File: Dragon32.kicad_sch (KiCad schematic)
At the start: 5 parts, among them IC25 LM393P, IC31 74LS02N

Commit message: rework board
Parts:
- IC31: value 74LS02N -> 74ACT02; footprint Package_DIP:DIP-14_W7.62mm -> Package_SO:SOIC-14_3.9x8.7mm_P1.27mm; DigiKey 296-1627-5-ND -> MC74ACT02DR2GOSCT-ND
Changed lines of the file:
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@@
       (effects (font (size 1.27 1.27)) (justify left))
     )
-    (property "Value" "74LS02N" (at 71.755 51.1809 0)
+    (property "Value" "74ACT02" (at 71.755 51.1809 0)
       (effects (font (size 1.27 1.27)) (justify left))
     )
-    (property "Footprint" "Package_DIP:DIP-14_W7.62mm" (at 65.913 49.911 0)
+    (property "Footprint" "Package_SO:SOIC-14_3.9x8.7mm_P1.27mm" (at 65.913 49.911 0)
       (effects (font (size 1.27 1.27)) hide)
     )
@@
       (effects (font (size 1.27 1.27)) hide)
     )
-    (property "DigiKey" "296-1627-5-ND" (at 65.913 49.911 0)
+    (property "DigiKey" "MC74ACT02DR2GOSCT-ND" (at 65.913 49.911 0)
       (effects (font (size 1.27 1.27)) hide)
     )

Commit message: serial wiring
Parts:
- IC1: renamed from IC25; value LM393P -> LM393DR; footprint Package_DIP:DIP-8_W7.62mm -> Package_SO:SOP-8_3.9x4.9mm_P1.27mm; DigiKey 296-1398-5-ND -> 296-1015-1-ND
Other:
- added sheet Serial (serial.kicad_sch)
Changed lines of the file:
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@@
   (symbol (lib_id "Comparator:LM393") (at 98.425 51.054 0) (unit 3)
     (in_bom yes) (on_board yes) (dnp no) (fields_autoplaced)
-    (property "Reference" "IC25" (at 96.52 49.7839 0)
-      (effects (font (size 1.27 1.27)) (justify left))
-    )
-    (property "Value" "LM393P" (at 96.52 52.3239 0)
-      (effects (font (size 1.27 1.27)) (justify left))
-    )
-    (property "Footprint" "Package_DIP:DIP-8_W7.62mm" (at 98.425 51.054 0)
+    (property "Reference" "IC1" (at 96.52 49.7839 0)
+      (effects (font (size 1.27 1.27)) (justify left))
+    )
+    (property "Value" "LM393DR" (at 96.52 52.3239 0)
+      (effects (font (size 1.27 1.27)) (justify left))
+    )
+    (property "Footprint" "Package_SO:SOP-8_3.9x4.9mm_P1.27mm" (at 98.425 51.054 0)
       (effects (font (size 1.27 1.27)) hide)
     )
@@
       (effects (font (size 1.27 1.27)) hide)
     )
-    (property "DigiKey" "296-1398-5-ND" (at 98.425 51.054 0)
+    (property "DigiKey" "296-1015-1-ND" (at 98.425 51.054 0)
       (effects (font (size 1.27 1.27)) hide)
     )
@@
       (project "Dragon32"
         (path "/0c3dceba-7c95-4b3d-b590-0eb581444beb"
-          (reference "IC25") (unit 3)
+          (reference "IC1") (unit 3)
         )
       )
@@
       (effects (font (size 1.27 1.27)) (justify left top))
     )
+    (instances
+      (project "Dragon32"
+        (path "/0c3dceba-7c95-4b3d-b590-0eb581444beb" (page "8"))
+      )
+    )
+  )
+  (sheet (at 361.188 184.15) (size 26.924 19.812) (fields_autoplaced)
+    (stroke (width 0.1524) (type solid))
+    (fill (color 0 0 0 0.0000))
+    (property "Sheetname" "Serial" (at 361.188 183.4384 0)
+      (effects (font (size 1.27 1.27)) (justify left bottom))
+    )
+    (property "Sheetfile" "serial.kicad_sch" (at 361.188 204.5466 0)
+      (effects (font (size 1.27 1.27)) (justify left top))
+    )

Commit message: add audio circuits
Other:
- added sheet AUDIO (audio.kicad_sch)
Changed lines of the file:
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@@
+    )
+  )
+  (sheet (at 361.188 151.892) (size 26.924 22.352) (fields_autoplaced)
+    (stroke (width 0.1524) (type solid))
+    (fill (color 0 0 0 0.0000))
+    (property "Sheetname" "AUDIO" (at 361.188 151.1804 0)
+      (effects (font (size 1.27 1.27)) (justify left bottom))
+    )
+    (property "Sheetfile" "audio.kicad_sch" (at 361.188 174.8286 0)
+      (effects (font (size 1.27 1.27)) (justify left top))
+    )
+    (instances
+      (project "Dragon32"
+        (path "/0c3dceba-7c95-4b3d-b590-0eb581444beb" (page "9"))
+      )
     )
   )

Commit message: update page info
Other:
- title: Dragon 32 CPU UK PAL -> Dragon 32 CPU RevX4
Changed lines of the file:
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@@
   (paper "A3")
   (title_block
-    (title "Dragon 32 CPU UK PAL")
-    (date "2023-05-25")
+    (title "Dragon 32 CPU RevX4")
+    (date "2024-01-07")
     (rev "3.0")
     (company "Dragon Data")

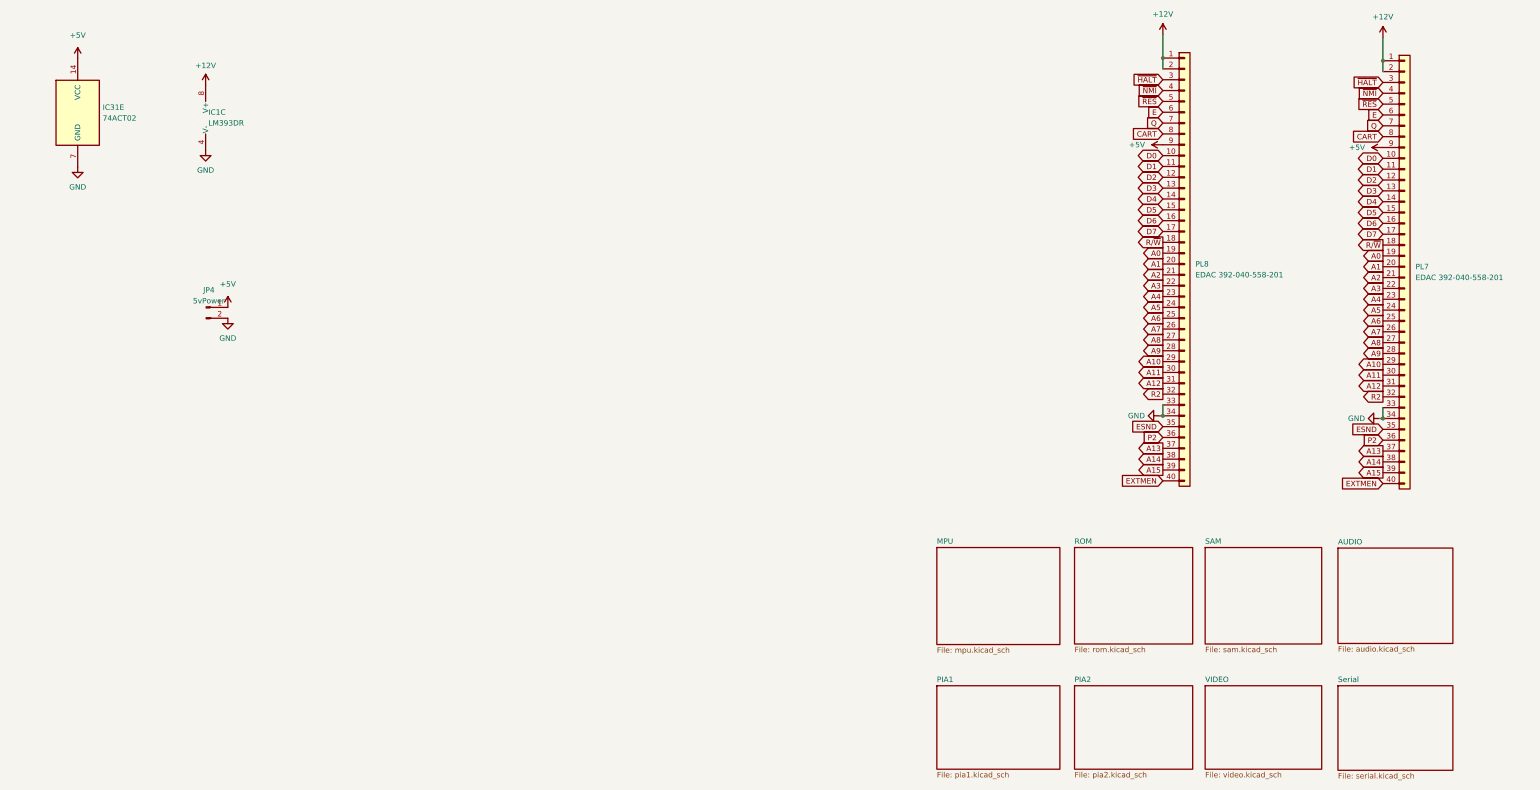
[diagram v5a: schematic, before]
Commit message: switch to fpga
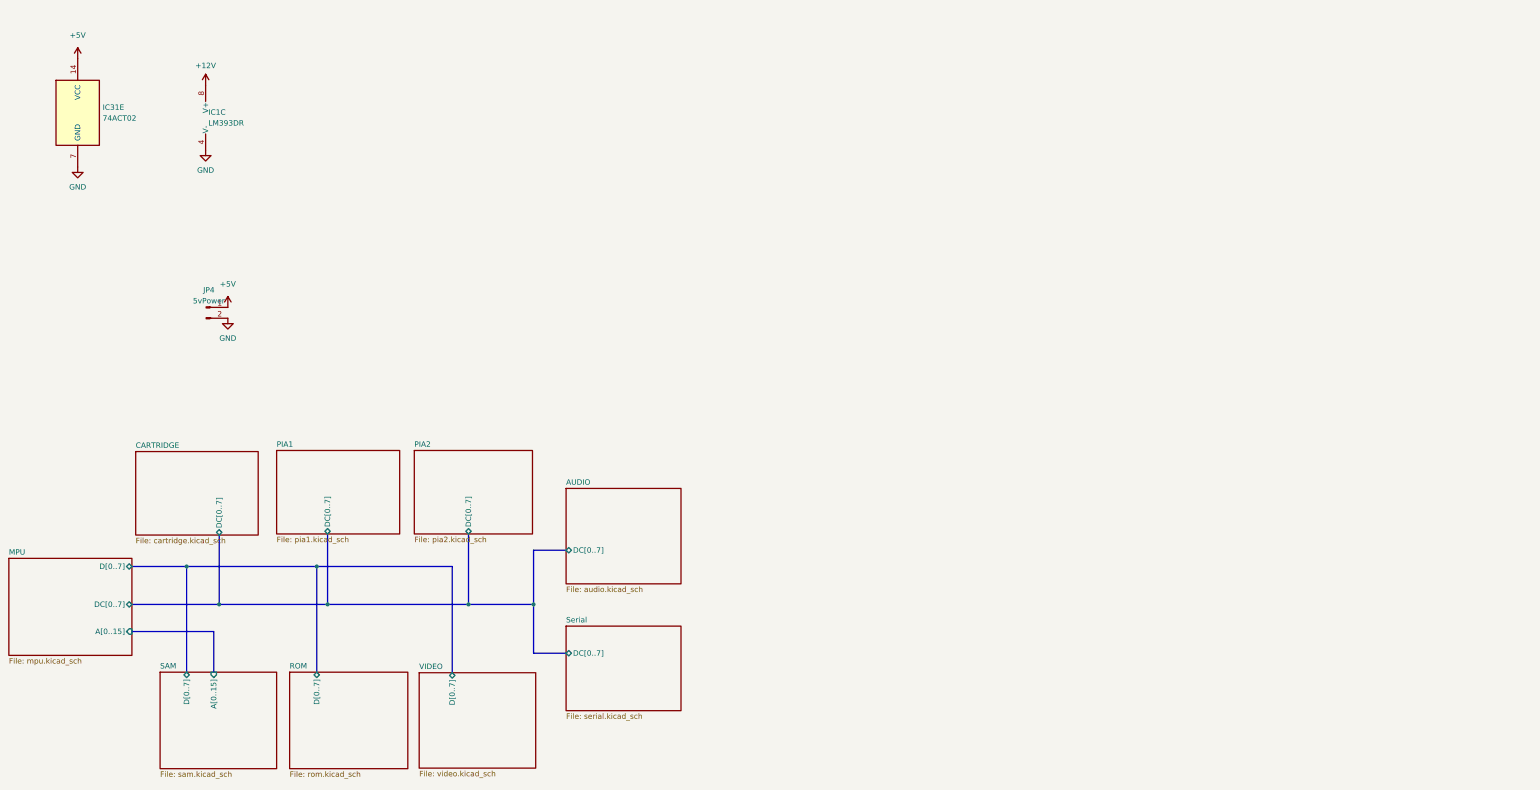
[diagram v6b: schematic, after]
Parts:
- removed PL7: EDAC 392-040-558-201, Dragon:Edge_2x20_P2.54mm_OvalMP, symbol Connector_Generic:Conn_01x40
- removed PL8: EDAC 392-040-558-201, Connector_PinHeader_2.54mm:PinHeader_2x20_P2.54mm_Vertical, symbol Connector_Generic:Conn_01x40
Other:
- added sheet CARTRIDGE (cartridge.kicad_sch)
- sheet AUDIO ports: added DC[0..7]; removed none
- sheet MPU ports: added A[0..15], DC[0..7], D[0..7]; removed none
- sheet PIA1 ports: added DC[0..7]; removed none
- sheet PIA2 ports: added DC[0..7]; removed none
- sheet ROM ports: added D[0..7]; removed none
- sheet SAM ports: added A[0..15], D[0..7]; removed none
- sheet Serial ports: added DC[0..7]; removed none
- sheet VIDEO ports: added D[0..7]; removed none
